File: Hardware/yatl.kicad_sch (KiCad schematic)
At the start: 19 parts, among them J1 Conn_01x08_Male, J2 Conn_01x08_Male, SW1 SW_SPST, U2 ATmega328-A

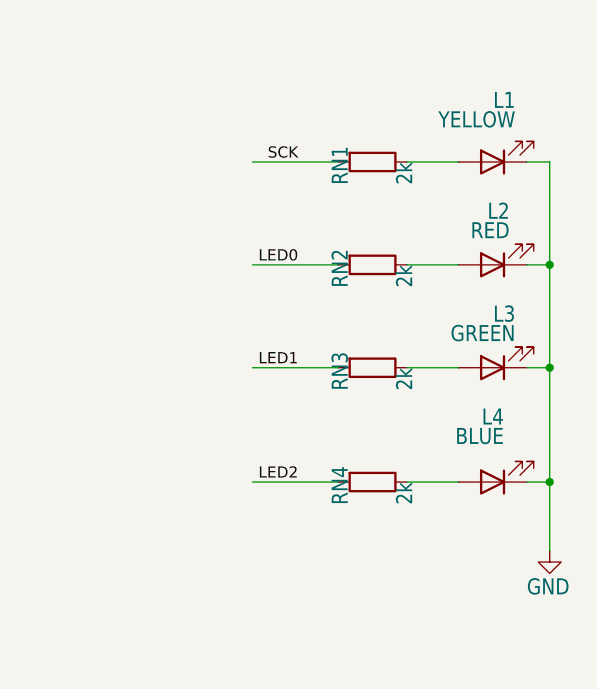
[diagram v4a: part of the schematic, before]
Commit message: Increase LED resistor value to reduce current consumption
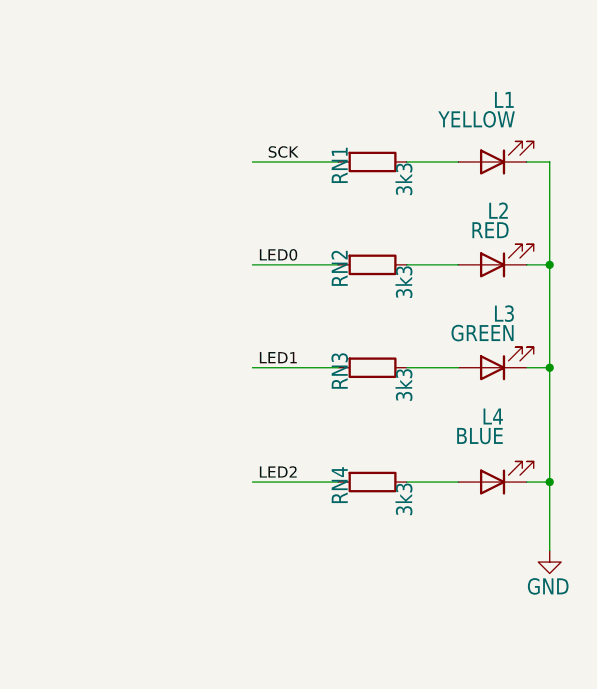
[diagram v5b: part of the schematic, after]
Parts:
- RN1, RN2, RN3, RN4: value 2k -> 3k3
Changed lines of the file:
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@@
       (effects (font (size 1.778 1.5113)) (justify right top))
     )
-    (property "Value" "2k" (id 1) (at 252.095 49.53 0)
+    (property "Value" "3k3" (id 1) (at 252.095 49.53 0)
       (effects (font (size 1.778 1.5113)) (justify left bottom))
     )
@@
       (effects (font (size 1.778 1.5113)) (justify right top))
     )
-    (property "Value" "2k" (id 1) (at 252.095 72.39 0)
+    (property "Value" "3k3" (id 1) (at 252.095 72.39 0)
       (effects (font (size 1.778 1.5113)) (justify left bottom))
     )
@@
       (effects (font (size 1.778 1.5113)) (justify right top))
     )
-    (property "Value" "2k" (id 1) (at 252.095 85.09 0)
+    (property "Value" "3k3" (id 1) (at 252.095 85.09 0)
       (effects (font (size 1.778 1.5113)) (justify left bottom))
     )
@@
       (effects (font (size 1.778 1.5113)) (justify right top))
     )
-    (property "Value" "2k" (id 1) (at 252.095 60.96 0)
+    (property "Value" "3k3" (id 1) (at 252.095 60.96 0)
       (effects (font (size 1.778 1.5113)) (justify left bottom))
     )
@@
     )
     (path "/420d34b4-3010-4c28-8f50-a13c623352af"
-      (reference "RN1") (unit 1) (value "2k") (footprint "Resistor_SMD:R_1206_3216Metric_Pad1.30x1.75mm_HandSolder")
+      (reference "RN1") (unit 1) (value "3k3") (footprint "Resistor_SMD:R_1206_3216Metric_Pad1.30x1.75mm_HandSolder")
     )
     (path "/9b482881-99f9-46bd-af4b-dc2db24183ee"
-      (reference "RN2") (unit 1) (value "2k") (footprint "Resistor_SMD:R_1206_3216Metric_Pad1.30x1.75mm_HandSolder")
+      (reference "RN2") (unit 1) (value "3k3") (footprint "Resistor_SMD:R_1206_3216Metric_Pad1.30x1.75mm_HandSolder")
     )
     (path "/44dbc5af-18b7-4b4a-9fbe-0fe74ab32e9f"
-      (reference "RN3") (unit 1) (value "2k") (footprint "Resistor_SMD:R_1206_3216Metric_Pad1.30x1.75mm_HandSolder")
+      (reference "RN3") (unit 1) (value "3k3") (footprint "Resistor_SMD:R_1206_3216Metric_Pad1.30x1.75mm_HandSolder")
     )
     (path "/7ed16553-8d73-4724-bcd1-39d97f91cb58"
-      (reference "RN4") (unit 1) (value "2k") (footprint "Resistor_SMD:R_1206_3216Metric_Pad1.30x1.75mm_HandSolder")
+      (reference "RN4") (unit 1) (value "3k3") (footprint "Resistor_SMD:R_1206_3216Metric_Pad1.30x1.75mm_HandSolder")
     )
     (path "/7d08da0b-aa56-4fd0-9e56-1760b10fa4de"

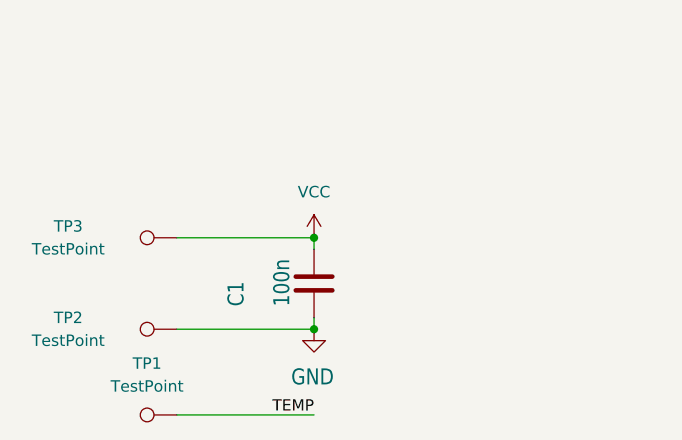
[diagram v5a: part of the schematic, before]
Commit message: Remove LMT86 decoupling capacitor that cause sudden temperature spike after certain minutes
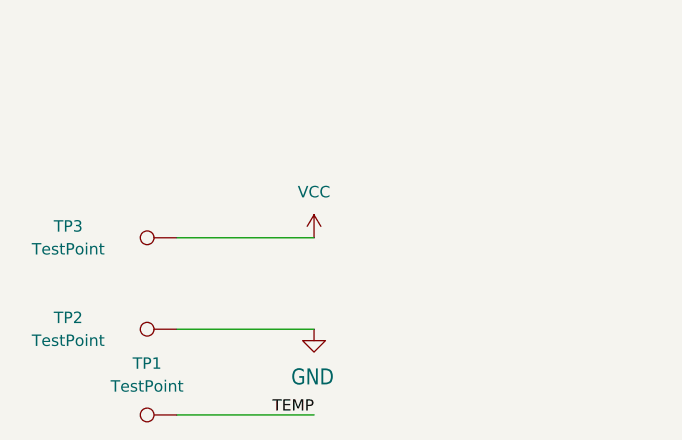
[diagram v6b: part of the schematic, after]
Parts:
- removed C1: 100n, Capacitor_SMD:C_1206_3216Metric_Pad1.33x1.80mm_HandSolder, symbol Device:C
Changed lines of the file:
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@@
   (junction (at 163.068 26.67) (diameter 0) (color 0 0 0 0)
   )
-  (junction (at 62.23 154.94) (diameter 0) (color 0 0 0 0)
-  )
   (junction (at 163.195 26.797) (diameter 0) (color 0 0 0 0)
   )
@@
   )
   (junction (at 269.24 85.09) (diameter 0) (color 0 0 0 0)
-  )
-  (junction (at 62.23 144.78) (diameter 0) (color 0 0 0 0)
   )
   (no_connect (at 178.435 59.69))
@@
     (stroke (width 0) (type default) (color 0 0 0 0))
   )
-  (wire (pts (xy 62.23 144.78) (xy 62.23 146.05))
-    (stroke (width 0) (type default) (color 0 0 0 0))
-  )
   (wire (pts (xy 269.24 72.39) (xy 269.24 85.09))
     (stroke (width 0) (type default) (color 0 0 0 0))
@@
   )
   (wire (pts (xy 67.31 36.83) (xy 49.53 36.83))
-    (stroke (width 0) (type default) (color 0 0 0 0))
-  )
-  (wire (pts (xy 62.23 153.67) (xy 62.23 154.94))
     (stroke (width 0) (type default) (color 0 0 0 0))
   )
@@
     )
     (property "Datasheet" "~" (id 3) (at 137.795 33.655 0)
-      (effects (font (size 1.27 1.27)) hide)
-    )
-    (pin "1")
-    (pin "2")
-  )
-  (symbol (lib_id "Device:C") (at 62.23 149.86 0) (unit 1)
-    (in_bom yes) (on_board yes)
-    (property "Reference" "C1" (id 0) (at 54.61 152.4 90)
-      (effects (font (size 1.778 1.5113)) (justify left bottom))
-    )
-    (property "Value" "100n" (id 1) (at 59.69 152.4 90)
-      (effects (font (size 1.778 1.5113)) (justify left bottom))
-    )
-    (property "Footprint" "Capacitor_SMD:C_1206_3216Metric_Pad1.33x1.80mm_HandSolder" (id 2) (at 63.1952 153.67 0)
-      (effects (font (size 1.27 1.27)) hide)
-    )
-    (property "Datasheet" "~" (id 3) (at 62.23 149.86 0)
       (effects (font (size 1.27 1.27)) hide)
     )
@@
       (reference "BT1") (unit 1) (value "Battery_Cell") (footprint "Battery:BatteryHolder_Keystone_3034_1x20mm")
     )
-    (path "/b3e5909d-9e99-4335-a49d-7bc57753a70d"
-      (reference "C1") (unit 1) (value "100n") (footprint "Capacitor_SMD:C_1206_3216Metric_Pad1.33x1.80mm_HandSolder")
-    )
     (path "/b0ab3db9-6698-4836-8d65-952a28319aa4"
